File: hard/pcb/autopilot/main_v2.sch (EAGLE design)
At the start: 167 parts, among them IC1 24AA32ASN, IC2 INA194, IC3 LP2950Z, Q1 IRLML5203, Q3 IRLML5203, Q4 IRLML5203, T3 BC848, U2 TMP75DGK, U44 BMP085, X1 USB-SMD-NS

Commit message: board v2 nop
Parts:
- removed C51: 10uF/16v, SparkFun:CAP_POL1206-KIT
- added F1: POLYSWITCH, barthess:POLYSWITCH
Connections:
- new net N$36: D2.C, F1.1
- net 6V: now also F1.2; no longer D2.C
- net GND_A: no longer C51.-
- net N$55: no longer C51.+
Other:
- moved on the sheet: C55, D2, IC3
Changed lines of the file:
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@@
 <part name="R57" library="SparkFun" deviceset="RESISTOR" device="0805-RES" value="1k"/>
 <part name="U$13" library="barthess" deviceset="6V" device=""/>
-<part name="C51" library="SparkFun" deviceset="CAP_POL" device="1206-KIT" value="10uF/16v"/>
 <part name="C52" library="SparkFun" deviceset="CAP_POL" device="1206-KIT" value="10uF/6.3v"/>
 <part name="U$5" library="barthess" deviceset="6V" device=""/>
@@
 <part name="C43" library="SparkFun" deviceset="CAP" device="0805" value="2.2uF"/>
 <part name="R6" library="barthess" deviceset="RESISTOR" device="1206" value="0"/>
+<part name="F1" library="barthess" deviceset="POLYSWITCH" device=""/>
 </parts>
 <sheets>
@@
 <instance part="R57" gate="G$1" x="91.44" y="-58.42" rot="R90"/>
 <instance part="U$13" gate="6V" x="127" y="-48.26" rot="R270"/>
-<instance part="C51" gate="G$1" x="-266.7" y="-106.68"/>
 <instance part="C52" gate="G$1" x="-218.44" y="-106.68"/>
 <instance part="U$5" gate="6V" x="-269.24" y="12.7"/>
@@
 <instance part="R59" gate="G$1" x="-292.1" y="-86.36" rot="R270"/>
 <instance part="C54" gate="G$1" x="-281.94" y="-96.52"/>
-<instance part="C55" gate="G$1" x="-248.92" y="-109.22"/>
-<instance part="IC3" gate="G$1" x="-236.22" y="-101.6"/>
+<instance part="C55" gate="G$1" x="-266.7" y="-109.22"/>
+<instance part="IC3" gate="G$1" x="-243.84" y="-101.6"/>
 <instance part="U$7" gate="G$1" x="198.12" y="96.52" rot="MR180"/>
 <instance part="P+23" gate="G$1" x="213.36" y="99.06" rot="MR90"/>
@@
 <instance part="R61" gate="G$1" x="-312.42" y="-96.52" rot="R180"/>
 <instance part="U$1" gate="6V" x="114.3" y="152.4"/>
-<instance part="D2" gate="G$1" x="-279.4" y="5.08"/>
+<instance part="D2" gate="G$1" x="-320.04" y="5.08"/>
 <instance part="F3" gate="G$1" x="-304.8" y="-2.54"/>
 <instance part="D3" gate="G$1" x="-289.56" y="-10.16"/>
@@
 <instance part="C43" gate="G$1" x="332.74" y="-254"/>
 <instance part="R6" gate="G$1" x="-195.58" y="-91.44"/>
+<instance part="F1" gate="G$1" x="-304.8" y="5.08"/>
 </instances>
 <busses>
@@
 </segment>
 <segment>
-<wire x1="-281.94" y1="5.08" x2="-287.02" y2="5.08" width="0.1524" layer="91"/>
-<label x="-287.02" y="5.08" size="1.27" layer="95" rot="R180" xref="yes"/>
+<wire x1="-322.58" y1="5.08" x2="-332.74" y2="5.08" width="0.1524" layer="91"/>
+<label x="-332.74" y="5.08" size="1.27" layer="95" rot="R180" xref="yes"/>
 <pinref part="D2" gate="G$1" pin="A"/>
 </segment>
@@
 <wire x1="-246.38" y1="-2.54" x2="-256.54" y2="-2.54" width="0.1524" layer="91"/>
 <wire x1="-256.54" y1="-2.54" x2="-269.24" y2="-2.54" width="0.1524" layer="91"/>
-<wire x1="-276.86" y1="5.08" x2="-269.24" y2="5.08" width="0.1524" layer="91"/>
+<wire x1="-297.18" y1="5.08" x2="-269.24" y2="5.08" width="0.1524" layer="91"/>
 <wire x1="-269.24" y1="5.08" x2="-269.24" y2="-2.54" width="0.1524" layer="91"/>
 <wire x1="-289.56" y1="-2.54" x2="-297.18" y2="-2.54" width="0.1524" layer="91"/>
@@
 <junction x="-289.56" y="-2.54"/>
 <junction x="-269.24" y="5.08"/>
-<pinref part="D2" gate="G$1" pin="C"/>
 <pinref part="F3" gate="G$1" pin="2"/>
 <pinref part="D3" gate="G$1" pin="C"/>
@@
 <wire x1="-256.54" y1="-7.62" x2="-256.54" y2="-2.54" width="0.1524" layer="91"/>
 <junction x="-256.54" y="-2.54"/>
+<pinref part="F1" gate="G$1" pin="2"/>
 </segment>
 <segment>
@@
 <net name="N$55" class="0">
 <segment>
-<wire x1="-243.84" y1="-99.06" x2="-248.92" y2="-99.06" width="0.1524" layer="91"/>
-<wire x1="-248.92" y1="-99.06" x2="-266.7" y2="-99.06" width="0.1524" layer="91"/>
+<wire x1="-251.46" y1="-99.06" x2="-266.7" y2="-99.06" width="0.1524" layer="91"/>
 <wire x1="-266.7" y1="-99.06" x2="-281.94" y2="-99.06" width="0.1524" layer="91"/>
 <junction x="-266.7" y="-99.06"/>
@@
 <pinref part="Q1" gate="G$1" pin="D"/>
 <pinref part="C54" gate="G$1" pin="2"/>
-<pinref part="C51" gate="G$1" pin="+"/>
+<pinref part="C55" gate="G$1" pin="1"/>
 <wire x1="-266.7" y1="-104.14" x2="-266.7" y2="-99.06" width="0.1524" layer="91"/>
-<pinref part="C55" gate="G$1" pin="1"/>
-<wire x1="-248.92" y1="-104.14" x2="-248.92" y2="-99.06" width="0.1524" layer="91"/>
-<junction x="-248.92" y="-99.06"/>
+<junction x="-266.7" y="-99.06"/>
 </segment>
 </net>
@@
 <wire x1="-218.44" y1="-111.76" x2="-218.44" y2="-114.3" width="0.1524" layer="91"/>
 <pinref part="C52" gate="G$1" pin="-"/>
-<wire x1="-236.22" y1="-109.22" x2="-236.22" y2="-114.3" width="0.1524" layer="91"/>
+<wire x1="-243.84" y1="-109.22" x2="-243.84" y2="-114.3" width="0.1524" layer="91"/>
 <pinref part="IC3" gate="G$1" pin="GND"/>
-<wire x1="-218.44" y1="-114.3" x2="-236.22" y2="-114.3" width="0.1524" layer="91"/>
-<wire x1="-266.7" y1="-114.3" x2="-266.7" y2="-111.76" width="0.1524" layer="91"/>
-<pinref part="C51" gate="G$1" pin="-"/>
-<wire x1="-236.22" y1="-114.3" x2="-248.92" y2="-114.3" width="0.1524" layer="91"/>
-<junction x="-236.22" y="-114.3"/>
-<junction x="-266.7" y="-114.3"/>
-<wire x1="-248.92" y1="-114.3" x2="-266.7" y2="-114.3" width="0.1524" layer="91"/>
+<wire x1="-218.44" y1="-114.3" x2="-243.84" y2="-114.3" width="0.1524" layer="91"/>
+<wire x1="-243.84" y1="-114.3" x2="-266.7" y2="-114.3" width="0.1524" layer="91"/>
+<junction x="-243.84" y="-114.3"/>
 <wire x1="-299.72" y1="-114.3" x2="-299.72" y2="-101.6" width="0.1524" layer="91"/>
 <pinref part="T3" gate="G$1" pin="E"/>
@@
 <junction x="-213.36" y="-73.66"/>
 <pinref part="C55" gate="G$1" pin="2"/>
-<wire x1="-248.92" y1="-111.76" x2="-248.92" y2="-114.3" width="0.1524" layer="91"/>
-<junction x="-248.92" y="-114.3"/>
+<wire x1="-266.7" y1="-111.76" x2="-266.7" y2="-114.3" width="0.1524" layer="91"/>
+<junction x="-266.7" y="-114.3"/>
 <pinref part="R6" gate="G$1" pin="1"/>
 </segment>
@@
 <net name="+5V_A" class="1">
 <segment>
-<wire x1="-218.44" y1="-99.06" x2="-228.6" y2="-99.06" width="0.1524" layer="91"/>
+<wire x1="-218.44" y1="-99.06" x2="-236.22" y2="-99.06" width="0.1524" layer="91"/>
 <wire x1="-218.44" y1="-104.14" x2="-218.44" y2="-99.06" width="0.1524" layer="91"/>
 <wire x1="-218.44" y1="-96.52" x2="-218.44" y2="-99.06" width="0.1524" layer="91"/>
@@
 </segment>
 </net>
+<net name="N$36" class="0">
+<segment>
+<pinref part="D2" gate="G$1" pin="C"/>
+<wire x1="-317.5" y1="5.08" x2="-309.88" y2="5.08" width="0.1524" layer="91"/>
+<pinref part="F1" gate="G$1" pin="1"/>
+</segment>
+</net>

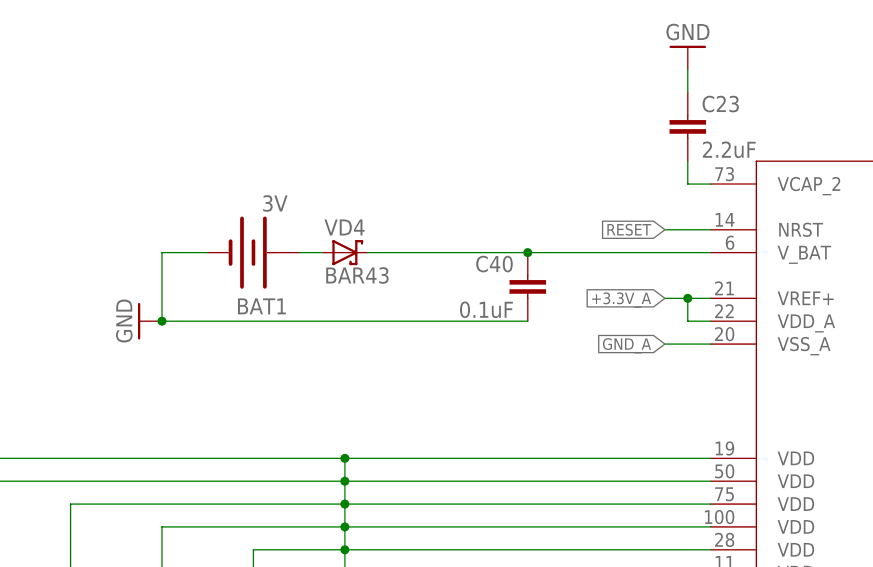
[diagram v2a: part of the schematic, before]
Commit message: board v2. Added capacitor for ADC
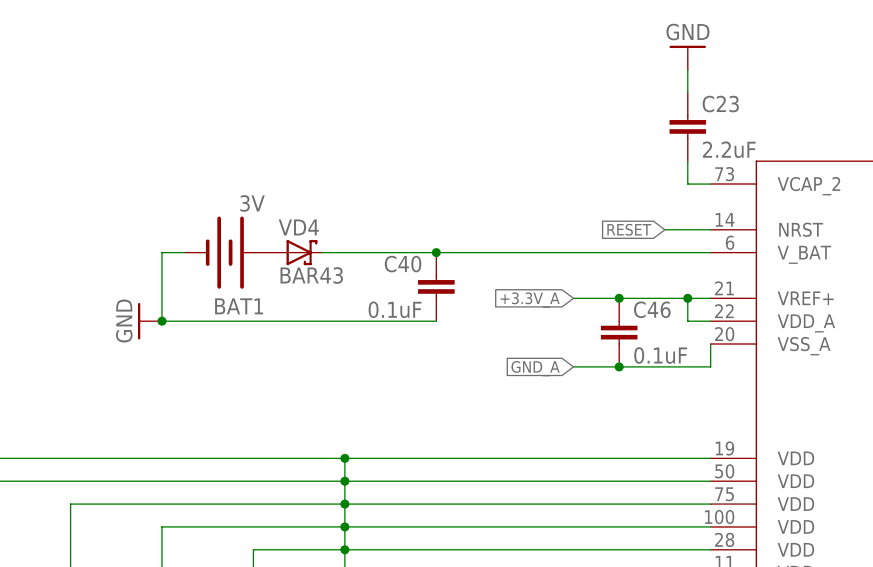
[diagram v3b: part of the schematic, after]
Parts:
- added C46: 0.1uF, SparkFun:CAP0805
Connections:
- net +3.3V_A: now also C46.1
- net GND_A: now also C46.2
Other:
- moved on the sheet: BAT1, C40, VD4
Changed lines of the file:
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@@
 <part name="R6" library="barthess" deviceset="RESISTOR" device="1206" value="0"/>
 <part name="F1" library="barthess" deviceset="POLYSWITCH" device=""/>
+<part name="C46" library="SparkFun" deviceset="CAP" device="0805" value="0.1uF"/>
 </parts>
 <sheets>
@@
 <instance part="GND32" gate="1" x="287.02" y="7.62"/>
 <instance part="P+19" gate="G$1" x="284.48" y="20.32" rot="R90"/>
-<instance part="BAT1" gate="G$1" x="-83.82" y="68.58" rot="R180"/>
+<instance part="BAT1" gate="G$1" x="-86.36" y="68.58" rot="R180"/>
 <instance part="VD8" gate="G$1" x="129.54" y="139.7" rot="R90"/>
 <instance part="XP2" gate="G$1" x="109.22" y="142.24" rot="MR270"/>
@@
 <instance part="GND20" gate="1" x="287.02" y="-226.06"/>
 <instance part="P+8" gate="G$1" x="289.56" y="-208.28"/>
-<instance part="VD4" gate="1" x="-73.66" y="68.58"/>
-<instance part="C40" gate="G$1" x="-53.34" y="63.5" rot="MR0"/>
+<instance part="VD4" gate="1" x="-78.74" y="68.58"/>
+<instance part="C40" gate="G$1" x="-63.5" y="63.5" rot="MR0"/>
 <instance part="JP6" gate="G$1" x="198.12" y="195.58"/>
 <instance part="P+22" gate="G$1" x="185.42" y="200.66"/>
@@
 <instance part="R6" gate="G$1" x="-195.58" y="-91.44"/>
 <instance part="F1" gate="G$1" x="-304.8" y="5.08"/>
+<instance part="C46" gate="G$1" x="-43.18" y="58.42"/>
 </instances>
 <busses>
@@
 <pinref part="BAT1" gate="G$1" pin="-"/>
 <pinref part="C40" gate="G$1" pin="2"/>
-<wire x1="-53.34" y1="60.96" x2="-93.98" y2="60.96" width="0.1524" layer="91"/>
+<wire x1="-63.5" y1="60.96" x2="-93.98" y2="60.96" width="0.1524" layer="91"/>
 <junction x="-93.98" y="60.96"/>
 <wire x1="-93.98" y1="60.96" x2="-93.98" y2="68.58" width="0.1524" layer="91"/>
-<wire x1="-93.98" y1="68.58" x2="-88.9" y2="68.58" width="0.1524" layer="91"/>
+<wire x1="-93.98" y1="68.58" x2="-91.44" y2="68.58" width="0.1524" layer="91"/>
 </segment>
 <segment>
@@
 <segment>
 <wire x1="-33.02" y1="63.5" x2="-35.56" y2="63.5" width="0.1524" layer="91"/>
-<label x="-38.1" y="63.5" size="1.27" layer="95" rot="R180" xref="yes"/>
+<label x="-48.26" y="63.5" size="1.27" layer="95" rot="R180" xref="yes"/>
 <pinref part="DD1" gate="G$1" pin="VREF+"/>
 <pinref part="DD1" gate="G$1" pin="VDD_A"/>
-<wire x1="-35.56" y1="63.5" x2="-38.1" y2="63.5" width="0.1524" layer="91"/>
+<wire x1="-35.56" y1="63.5" x2="-43.18" y2="63.5" width="0.1524" layer="91"/>
+<wire x1="-43.18" y1="63.5" x2="-48.26" y2="63.5" width="0.1524" layer="91"/>
 <wire x1="-33.02" y1="60.96" x2="-35.56" y2="60.96" width="0.1524" layer="91"/>
 <wire x1="-35.56" y1="60.96" x2="-35.56" y2="63.5" width="0.1524" layer="91"/>
 <junction x="-35.56" y="63.5"/>
+<pinref part="C46" gate="G$1" pin="1"/>
+<junction x="-43.18" y="63.5"/>
 </segment>
 <segment>
@@
 <net name="GND_A" class="3">
 <segment>
-<label x="-38.1" y="58.42" size="1.27" layer="95" rot="R180" xref="yes"/>
+<label x="-48.26" y="55.88" size="1.27" layer="95" rot="R180" xref="yes"/>
 <pinref part="DD1" gate="G$1" pin="VSS_A"/>
-<wire x1="-33.02" y1="58.42" x2="-38.1" y2="58.42" width="0.1524" layer="91"/>
+<wire x1="-33.02" y1="58.42" x2="-33.02" y2="55.88" width="0.1524" layer="91"/>
+<wire x1="-33.02" y1="55.88" x2="-43.18" y2="55.88" width="0.1524" layer="91"/>
+<pinref part="C46" gate="G$1" pin="2"/>
+<junction x="-43.18" y="55.88"/>
+<wire x1="-43.18" y1="55.88" x2="-48.26" y2="55.88" width="0.1524" layer="91"/>
 </segment>
 <segment>
@@
 <pinref part="BAT1" gate="G$1" pin="+"/>
 <pinref part="VD4" gate="1" pin="A"/>
-<wire x1="-76.2" y1="68.58" x2="-78.74" y2="68.58" width="0.1524" layer="91"/>
 </segment>
 </net>
@@
 <segment>
 <pinref part="DD1" gate="G$1" pin="V_BAT"/>
-<wire x1="-33.02" y1="68.58" x2="-53.34" y2="68.58" width="0.1524" layer="91"/>
+<wire x1="-33.02" y1="68.58" x2="-63.5" y2="68.58" width="0.1524" layer="91"/>
 <pinref part="VD4" gate="1" pin="C"/>
 <pinref part="C40" gate="G$1" pin="1"/>
-<wire x1="-53.34" y1="68.58" x2="-71.12" y2="68.58" width="0.1524" layer="91"/>
-<junction x="-53.34" y="68.58"/>
-</segment>
-</net>
+<wire x1="-63.5" y1="68.58" x2="-76.2" y2="68.58" width="0.1524" layer="91"/>
+<junction x="-63.5" y="68.58"/>
+</segment>
+</net>

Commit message: nop
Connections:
- net I2C_FAST_SCL: now also DD1.PB10; no longer DD1.PB6
- net I2C_FAST_SDA: now also DD1.PB11; no longer DD1.PB7
- net I2C_SLOW_SCL: now also DD1.PB6; no longer DD1.PB10
- net I2C_SLOW_SDA: now also DD1.PB7; no longer DD1.PB11
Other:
- moved on the sheet: R11, R25, R27, R28
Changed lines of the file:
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@@
 <setting verticaltext="up"/>
 </settings>
-<grid distance="0.1" unitdist="inch" unit="inch" style="lines" multiple="1" display="no" altdistance="0.01" altunitdist="inch" altunit="inch"/>
+<grid distance="0.1" unitdist="inch" unit="inch" style="lines" multiple="1" display="yes" altdistance="0.01" altunitdist="inch" altunit="inch"/>
 <layers>
 <layer number="1" name="Top" color="4" fill="1" visible="no" active="no"/>
@@
 <instance part="P+18" gate="G$1" x="-218.44" y="2.54"/>
 <instance part="GND31" gate="1" x="-218.44" y="-20.32"/>
-<instance part="R27" gate="G$1" x="76.2" y="78.74" rot="R90"/>
-<instance part="P+16" gate="G$1" x="66.04" y="86.36"/>
-<instance part="R28" gate="G$1" x="66.04" y="76.2" rot="R90"/>
+<instance part="R27" gate="G$1" x="109.22" y="68.58" rot="R90"/>
+<instance part="P+16" gate="G$1" x="99.06" y="76.2"/>
+<instance part="R28" gate="G$1" x="99.06" y="66.04" rot="R90"/>
 <instance part="U44" gate="G$1" x="309.88" y="17.78"/>
 <instance part="U2" gate="G$1" x="309.88" y="-12.7"/>
@@
 <instance part="C37" gate="G$1" x="106.68" y="-55.88" rot="MR180"/>
 <instance part="C39" gate="G$1" x="86.36" y="-55.88" rot="MR180"/>
-<instance part="R11" gate="G$1" x="114.3" y="68.58" rot="R90"/>
-<instance part="P+20" gate="G$1" x="104.14" y="76.2"/>
-<instance part="R25" gate="G$1" x="104.14" y="66.04" rot="R90"/>
+<instance part="R11" gate="G$1" x="73.66" y="78.74" rot="R90"/>
+<instance part="P+20" gate="G$1" x="63.5" y="86.36"/>
+<instance part="R25" gate="G$1" x="63.5" y="76.2" rot="R90"/>
 <instance part="R26" gate="G$1" x="76.2" y="50.8" rot="MR0"/>
 <instance part="R37" gate="G$1" x="76.2" y="45.72" rot="MR0"/>
@@
 </segment>
 <segment>
-<wire x1="66.04" y1="86.36" x2="66.04" y2="83.82" width="0.1524" layer="91"/>
-<wire x1="66.04" y1="83.82" x2="66.04" y2="81.28" width="0.1524" layer="91"/>
-<wire x1="66.04" y1="83.82" x2="76.2" y2="83.82" width="0.1524" layer="91"/>
-<junction x="66.04" y="83.82"/>
+<wire x1="99.06" y1="76.2" x2="99.06" y2="73.66" width="0.1524" layer="91"/>
+<wire x1="99.06" y1="73.66" x2="99.06" y2="71.12" width="0.1524" layer="91"/>
+<wire x1="99.06" y1="73.66" x2="109.22" y2="73.66" width="0.1524" layer="91"/>
+<junction x="99.06" y="73.66"/>
 <pinref part="P+16" gate="G$1" pin="3.3V"/>
 <pinref part="R28" gate="G$1" pin="2"/>
@@
 </segment>
 <segment>
-<wire x1="104.14" y1="76.2" x2="104.14" y2="73.66" width="0.1524" layer="91"/>
-<wire x1="104.14" y1="73.66" x2="104.14" y2="71.12" width="0.1524" layer="91"/>
-<wire x1="104.14" y1="73.66" x2="114.3" y2="73.66" width="0.1524" layer="91"/>
-<junction x="104.14" y="73.66"/>
+<wire x1="63.5" y1="86.36" x2="63.5" y2="83.82" width="0.1524" layer="91"/>
+<wire x1="63.5" y1="83.82" x2="63.5" y2="81.28" width="0.1524" layer="91"/>
+<wire x1="63.5" y1="83.82" x2="73.66" y2="83.82" width="0.1524" layer="91"/>
+<junction x="63.5" y="83.82"/>
 <pinref part="P+20" gate="G$1" pin="3.3V"/>
 <pinref part="R25" gate="G$1" pin="2"/>
@@
 <net name="I2C_FAST_SCL" class="0">
 <segment>
-<wire x1="66.04" y1="71.12" x2="66.04" y2="68.58" width="0.1524" layer="91"/>
-<wire x1="66.04" y1="68.58" x2="81.28" y2="68.58" width="0.1524" layer="91"/>
-<label x="81.28" y="68.58" size="1.27" layer="95" xref="yes"/>
+<wire x1="99.06" y1="60.96" x2="99.06" y2="58.42" width="0.1524" layer="91"/>
+<wire x1="99.06" y1="58.42" x2="114.3" y2="58.42" width="0.1524" layer="91"/>
+<label x="114.3" y="58.42" size="1.27" layer="95" xref="yes"/>
 <pinref part="R28" gate="G$1" pin="1"/>
-<pinref part="DD1" gate="G$1" pin="PB6"/>
-<wire x1="66.04" y1="68.58" x2="40.64" y2="68.58" width="0.1524" layer="91"/>
-<junction x="66.04" y="68.58"/>
+<pinref part="DD1" gate="G$1" pin="PB10"/>
+<wire x1="99.06" y1="58.42" x2="40.64" y2="58.42" width="0.1524" layer="91"/>
+<junction x="99.06" y="58.42"/>
 </segment>
 <segment>
@@
 <net name="I2C_FAST_SDA" class="0">
 <segment>
-<wire x1="76.2" y1="73.66" x2="76.2" y2="66.04" width="0.1524" layer="91"/>
-<wire x1="76.2" y1="66.04" x2="81.28" y2="66.04" width="0.1524" layer="91"/>
-<label x="81.28" y="66.04" size="1.27" layer="95" xref="yes"/>
+<wire x1="109.22" y1="63.5" x2="109.22" y2="55.88" width="0.1524" layer="91"/>
+<wire x1="109.22" y1="55.88" x2="114.3" y2="55.88" width="0.1524" layer="91"/>
+<label x="114.3" y="55.88" size="1.27" layer="95" xref="yes"/>
 <pinref part="R27" gate="G$1" pin="1"/>
-<pinref part="DD1" gate="G$1" pin="PB7"/>
-<wire x1="76.2" y1="66.04" x2="40.64" y2="66.04" width="0.1524" layer="91"/>
-<junction x="76.2" y="66.04"/>
+<pinref part="DD1" gate="G$1" pin="PB11"/>
+<wire x1="109.22" y1="55.88" x2="40.64" y2="55.88" width="0.1524" layer="91"/>
+<junction x="109.22" y="55.88"/>
 </segment>
 <segment>
@@
 <net name="I2C_SLOW_SCL" class="0">
 <segment>
-<label x="116.84" y="58.42" size="1.27" layer="95" xref="yes"/>
+<label x="76.2" y="68.58" size="1.27" layer="95" xref="yes"/>
 <pinref part="R25" gate="G$1" pin="1"/>
-<wire x1="104.14" y1="58.42" x2="116.84" y2="58.42" width="0.1524" layer="91"/>
-<wire x1="104.14" y1="60.96" x2="104.14" y2="58.42" width="0.1524" layer="91"/>
-<junction x="104.14" y="58.42"/>
-<wire x1="104.14" y1="58.42" x2="40.64" y2="58.42" width="0.1524" layer="91"/>
-<pinref part="DD1" gate="G$1" pin="PB10"/>
+<wire x1="63.5" y1="68.58" x2="76.2" y2="68.58" width="0.1524" layer="91"/>
+<wire x1="63.5" y1="71.12" x2="63.5" y2="68.58" width="0.1524" layer="91"/>
+<pinref part="DD1" gate="G$1" pin="PB6"/>
+<wire x1="63.5" y1="68.58" x2="40.64" y2="68.58" width="0.1524" layer="91"/>
+<junction x="63.5" y="68.58"/>
 </segment>
 <segment>
@@
 <net name="I2C_SLOW_SDA" class="0">
 <segment>
-<label x="116.84" y="55.88" size="1.27" layer="95" xref="yes"/>
+<label x="76.2" y="66.04" size="1.27" layer="95" xref="yes"/>
 <pinref part="R11" gate="G$1" pin="1"/>
-<wire x1="114.3" y1="55.88" x2="116.84" y2="55.88" width="0.1524" layer="91"/>
-<wire x1="114.3" y1="63.5" x2="114.3" y2="55.88" width="0.1524" layer="91"/>
-<junction x="114.3" y="55.88"/>
-<wire x1="114.3" y1="55.88" x2="40.64" y2="55.88" width="0.1524" layer="91"/>
-<pinref part="DD1" gate="G$1" pin="PB11"/>
-</segment>
-<segment>
+<wire x1="73.66" y1="66.04" x2="76.2" y2="66.04" width="0.1524" layer="91"/>
+<wire x1="73.66" y1="73.66" x2="73.66" y2="66.04" width="0.1524" layer="91"/>
+<pinref part="DD1" gate="G$1" pin="PB7"/>
+<wire x1="73.66" y1="66.04" x2="40.64" y2="66.04" width="0.1524" layer="91"/>
+<junction x="73.66" y="66.04"/>
+</segment>
+<segment>
